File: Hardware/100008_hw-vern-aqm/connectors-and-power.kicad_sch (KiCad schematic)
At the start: 41 parts, among them J1 Conn_01x14_Socket, J2 USB4220-03-1000-C, J3 Conn_01x06_MountingPin, J4 Conn_01x03_Pin, J5 Conn_01x06_Socket, J6 Conn_01x04_Socket, J7 Conn_01x05_Pin, J8 Conn_01x04_MountingPin, U1 AMS1117-3.3

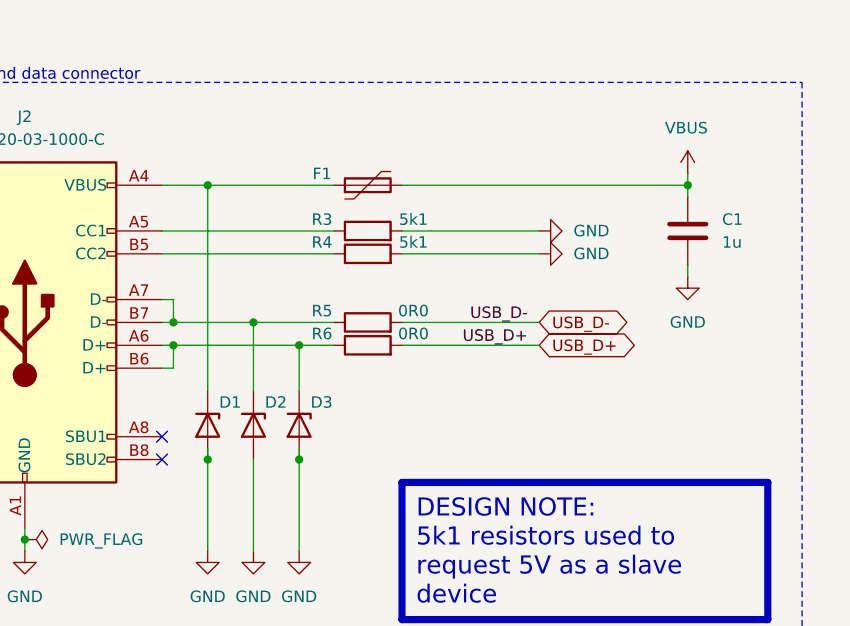
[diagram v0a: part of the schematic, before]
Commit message: fixing DRC issues
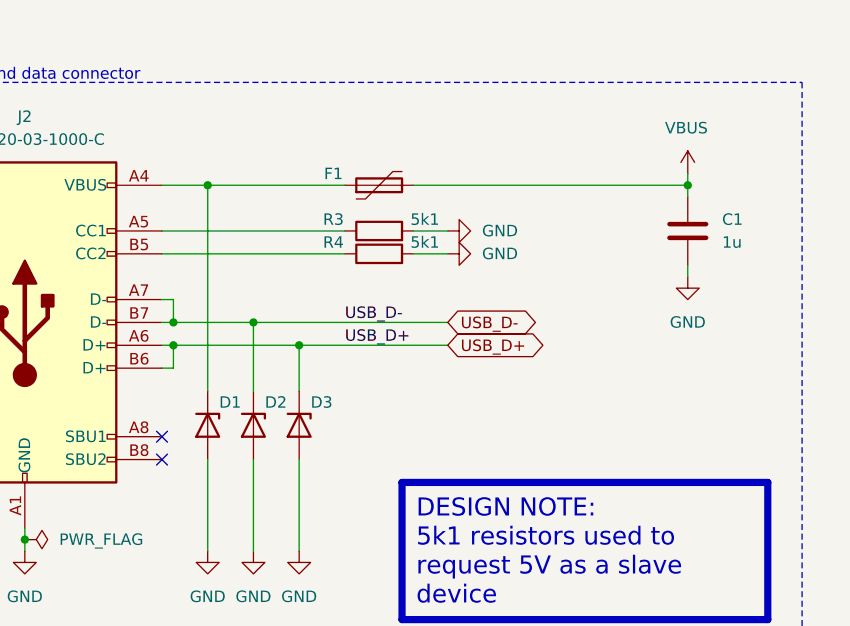
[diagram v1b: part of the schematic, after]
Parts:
- removed R5, R6: 0R0, Resistor_SMD:R_0603_1608Metric, symbol Device:R
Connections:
- net USB_D+: now also D3.1 (K), J2.A6 (D+), J2.B6 (D+)
- net USB_D-: now also D2.1 (K), J2.A7 (D-), J2.B7 (D-)
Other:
- moved on the sheet: F1, R3, R4

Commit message: schematic release, pcb release
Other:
- note removed: "AN5346"
- note removed: "J. Pieper ADC investigation"
- note removed: "STM32G474 Datasheet p.81"
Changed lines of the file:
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@@
-		)
-	)
-	(text "J. Pieper ADC investigation"
-		(exclude_from_sim no)
-		(at 266.7 259.08 0)
-		(effects
-			(font
-				(face "Arial")
-				(size 1.27 1.27)
-				(color 0 0 0 1)
-			)
-			(justify left bottom)
-			(href "https://jpieper.com/2023/07/24/stm32g4-adc-performance-part-2/")
 		)
 	)
@@
 		)
 	)
-	(text "STM32G474 Datasheet p.81"
-		(exclude_from_sim no)
-		(at 266.7 255.27 0)
-		(effects
-			(font
-				(face "Arial")
-				(size 1.27 1.27)
-				(color 0 0 0 1)
-			)
-			(justify left bottom)
-			(href "https://www.st.com/resource/en/datasheet/stm32g474cb.pdf")
-		)
-	)
-	(text "AN5346"
-		(exclude_from_sim no)
-		(at 266.7 251.46 0)
-		(effects
-			(font
-				(face "Arial")
-				(size 1.27 1.27)
-				(color 0 0 0 1)
-			)
-			(justify left bottom)
-			(href "https://www.st.com/resource/en/application_note/an5346-stm32g4-adc-use-tips-and-recommendations-stmicroelectronics.pdf")
-		)
-	)
